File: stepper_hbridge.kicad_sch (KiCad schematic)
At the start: 20 parts, among them Q1 AO4264E, Q2 AO4264E, Q3 AO4264E, Q4 AO4264E

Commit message: Added symbol library
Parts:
- C2: value (none) -> 2.2n 50V; footprint (none) -> Capacitor_SMD:C_0603_1608Metric
- C5: value (none) -> 4.7uF 100V; footprint (none) -> Capacitor_SMD:C_1210_3225Metric
- Q1, Q3, Q4: symbol PersonnalSymbolLibrary:AO4264E -> QuarkCncStepperDrivers:AO4264E
- Q2: value AO4264E -> (none); symbol PersonnalSymbolLibrary:AO4264E -> QuarkCncStepperDrivers:AO4264E
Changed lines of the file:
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@@
     (stroke (width 0) (type default) (color 0 0 0 0))
   )
-  (text "Size up to 1206" (at 95.25 48.26 0)
+  (text "Size up to 1206" (at 95.25 46.99 0)
     (effects (font (size 1.27 1.27)) (justify left bottom))
   )
@@
     (effects (font (size 1.27 1.27)) (justify left bottom))
   )
-  (text "Average Pdiss of\n sense resistor\n     0.1 W" (at 95.25 57.15 0)
+  (text "Average Pdiss of\n sense resistor\n     0.1 W" (at 95.25 55.88 0)
     (effects (font (size 1.27 1.27)) (justify left bottom))
   )
@@
       (effects (font (size 1.27 1.27)) (justify left))
     )
-    (property "Value" "" (id 1) (at 97.79 102.2349 0)
-      (effects (font (size 1.27 1.27)) (justify left))
-    )
-    (property "Footprint" "" (id 2) (at 94.9452 104.14 0)
+    (property "Value" "2.2n 50V" (id 1) (at 97.79 102.2349 0)
+      (effects (font (size 1.27 1.27)) (justify left))
+    )
+    (property "Footprint" "Capacitor_SMD:C_0603_1608Metric" (id 2) (at 94.9452 104.14 0)
       (effects (font (size 1.27 1.27)) hide)
     )
@@
     (pin "2")
   )
-  (symbol (lib_id "PersonnalSymbolLibrary:AO4264E") (at 113.03 80.01 0) (unit 1)
+  (symbol (lib_id "QuarkCncStepperDrivers:AO4264E") (at 113.03 80.01 0) (unit 1)
     (in_bom yes) (on_board yes)
     (property "Reference" "Q2" (id 0) (at 116.84 76.1999 0)
       (effects (font (size 1.27 1.27)) (justify left))
     )
-    (property "Value" "AO4264E" (id 1) (at 116.84 83.8199 0)
+    (property "Value" "" (id 1) (at 116.84 83.8199 0)
       (effects (font (size 1.27 1.27)) (justify left))
     )
@@
       (effects (font (size 1.27 1.27)) (justify left) hide)
     )
-    (property "LCSC" "C334232" (id 4) (at 104.14 85.0899 0)
-      (effects (font (size 1.27 1.27)) (justify left) hide)
+    (property "LCSC" "C334232" (id 4) (at 113.03 80.01 0)
+      (effects (font (size 1.27 1.27)) hide)
     )
     (pin "1")
@@
       (effects (font (size 1.27 1.27)) (justify left))
     )
-    (property "Value" "" (id 1) (at 175.26 59.0549 0)
-      (effects (font (size 1.27 1.27)) (justify left))
-    )
-    (property "Footprint" "" (id 2) (at 172.4152 60.96 0)
+    (property "Value" "4.7uF 100V" (id 1) (at 175.26 59.0549 0)
+      (effects (font (size 1.27 1.27)) (justify left))
+    )
+    (property "Footprint" "Capacitor_SMD:C_1210_3225Metric" (id 2) (at 172.4152 60.96 0)
       (effects (font (size 1.27 1.27)) hide)
     )
@@
     (pin "2")
   )
-  (symbol (lib_id "PersonnalSymbolLibrary:AO4264E") (at 113.03 64.77 0) (unit 1)
+  (symbol (lib_id "QuarkCncStepperDrivers:AO4264E") (at 113.03 64.77 0) (unit 1)
     (in_bom yes) (on_board yes)
     (property "Reference" "Q1" (id 0) (at 116.84 60.9599 0)
@@
       (effects (font (size 1.27 1.27)) (justify left) hide)
     )
-    (property "LCSC" "C334232" (id 4) (at 104.14 68.5799 0)
-      (effects (font (size 1.27 1.27)) (justify left) hide)
+    (property "LCSC" "C334232" (id 4) (at 113.03 64.77 0)
+      (effects (font (size 1.27 1.27)) hide)
     )
     (pin "1")
@@
     (pin "2")
   )
-  (symbol (lib_id "PersonnalSymbolLibrary:AO4264E") (at 149.86 64.77 0) (unit 1)
+  (symbol (lib_id "QuarkCncStepperDrivers:AO4264E") (at 149.86 64.77 0) (unit 1)
     (in_bom yes) (on_board yes)
     (property "Reference" "Q3" (id 0) (at 147.32 60.9599 0)
@@
       (effects (font (size 1.27 1.27)) (justify left) hide)
     )
-    (property "LCSC" "C334232" (id 4) (at 156.21 67.3099 0)
-      (effects (font (size 1.27 1.27)) (justify left) hide)
+    (property "LCSC" "C334232" (id 4) (at 149.86 64.77 0)
+      (effects (font (size 1.27 1.27)) hide)
     )
     (pin "1")
@@
     (pin "2")
   )
-  (symbol (lib_id "PersonnalSymbolLibrary:AO4264E") (at 149.86 80.01 0) (unit 1)
+  (symbol (lib_id "QuarkCncStepperDrivers:AO4264E") (at 149.86 80.01 0) (unit 1)
     (in_bom yes) (on_board yes)
     (property "Reference" "Q4" (id 0) (at 147.32 76.1999 0)
@@
       (effects (font (size 1.27 1.27)) (justify left) hide)
     )
-    (property "LCSC" "C334232" (id 4) (at 156.21 82.5499 0)
-      (effects (font (size 1.27 1.27)) (justify left) hide)
-    )
-    (pin "1")
+    (property "LCSC" "C334232" (id 4) (at 149.86 80.01 0)
+      (effects (font (size 1.27 1.27)) hide)
+    )
+    (pin "1")

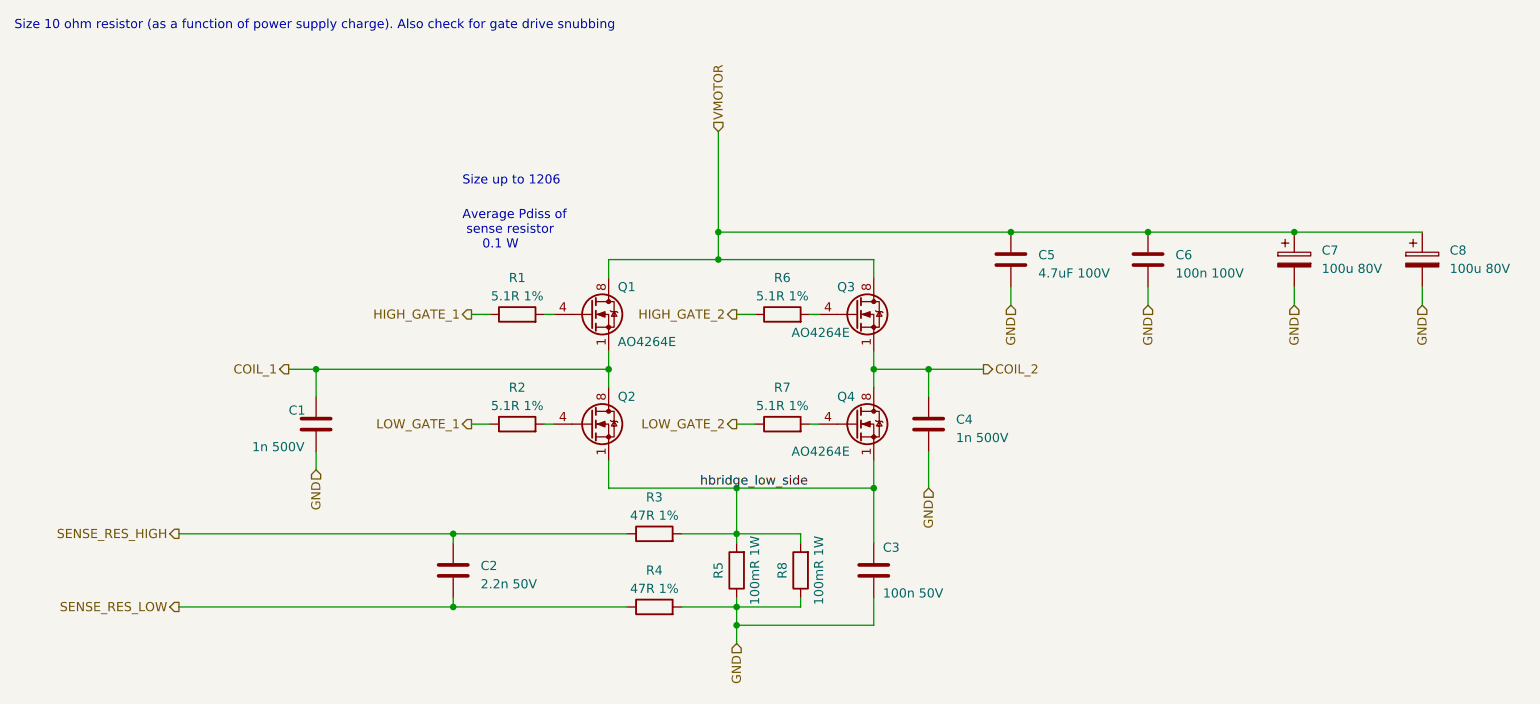
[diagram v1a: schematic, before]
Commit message: Removed caps from board. Will be placed on main board
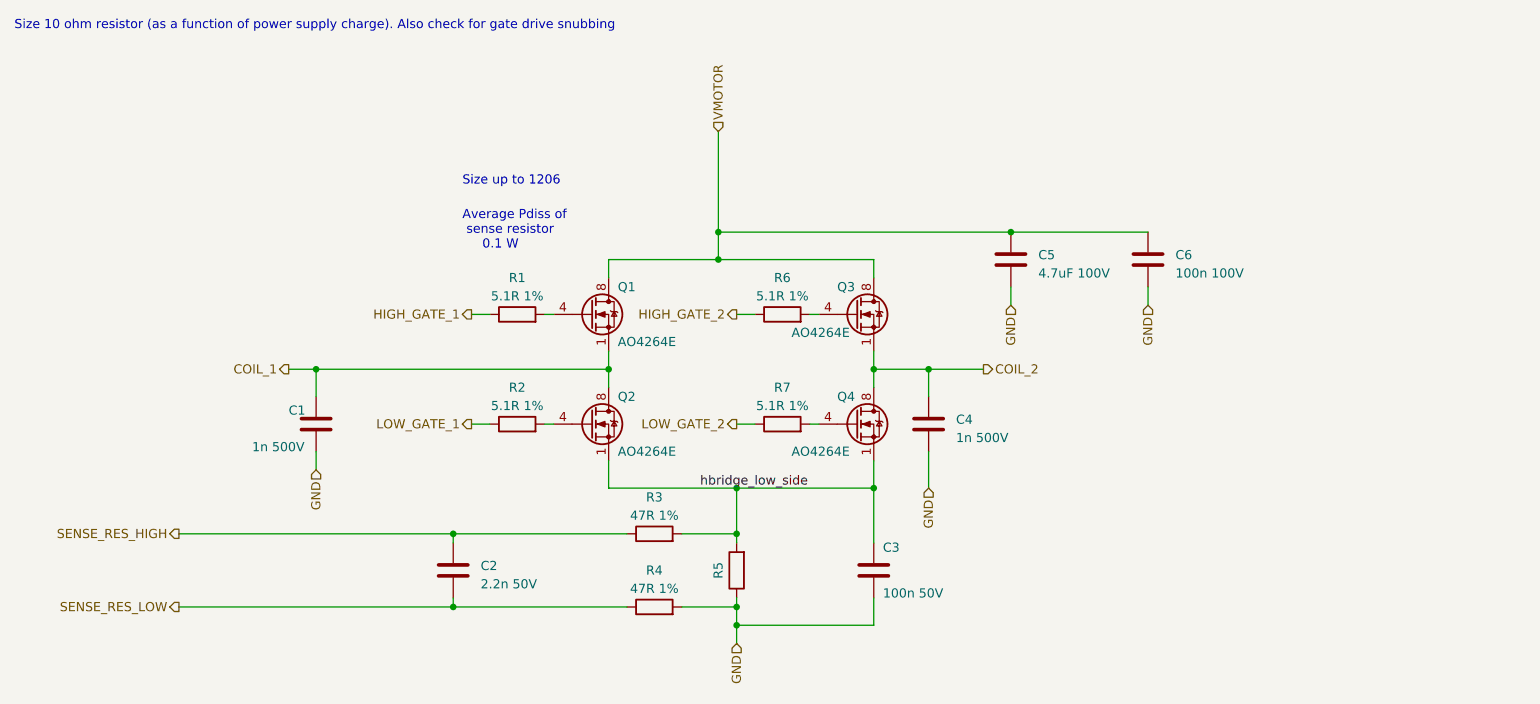
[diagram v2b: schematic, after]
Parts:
- removed C7, C8: 100u 80V, Capacitor_SMD:CP_Elec_10x10, symbol Device:C_Polarized
- removed R8: 100mR 1W, Resistor_SMD:R_1218_3246Metric, symbol Device:R
- Q2: value (none) -> AO4264E
- R5: value 100mR 1W -> (none); footprint Resistor_SMD:R_1218_3246Metric -> (none); LCSC C309639 -> C493478
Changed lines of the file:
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@@
   (junction (at 93.98 95.25) (diameter 0) (color 0 0 0 0)
   )
-  (junction (at 190.5 53.34) (diameter 0) (color 0 0 0 0)
-  )
   (junction (at 74.93 72.39) (diameter 0) (color 0 0 0 0)
   )
@@
   (junction (at 133.35 95.25) (diameter 0.9144) (color 0 0 0 0)
   )
-  (junction (at 210.82 53.34) (diameter 0) (color 0 0 0 0)
-  )
   (junction (at 93.98 105.41) (diameter 0) (color 0 0 0 0)
   )
@@
     (stroke (width 0) (type solid) (color 0 0 0 0))
   )
-  (wire (pts (xy 190.5 53.34) (xy 210.82 53.34))
-    (stroke (width 0) (type default) (color 0 0 0 0))
-  )
   (wire (pts (xy 130.81 57.15) (xy 152.4 57.15))
     (stroke (width 0) (type solid) (color 0 0 0 0))
   )
-  (wire (pts (xy 142.24 95.25) (xy 133.35 95.25))
-    (stroke (width 0) (type default) (color 0 0 0 0))
-  )
-  (wire (pts (xy 142.24 96.52) (xy 142.24 95.25))
-    (stroke (width 0) (type default) (color 0 0 0 0))
-  )
   (wire (pts (xy 115.57 57.15) (xy 130.81 57.15))
     (stroke (width 0) (type solid) (color 0 0 0 0))
@@
     (stroke (width 0) (type default) (color 0 0 0 0))
   )
-  (wire (pts (xy 210.82 53.34) (xy 228.6 53.34))
-    (stroke (width 0) (type default) (color 0 0 0 0))
-  )
   (wire (pts (xy 125.73 95.25) (xy 133.35 95.25))
     (stroke (width 0) (type solid) (color 0 0 0 0))
   )
-  (wire (pts (xy 228.6 60.96) (xy 228.6 63.5))
-    (stroke (width 0) (type default) (color 0 0 0 0))
-  )
   (wire (pts (xy 55.88 105.41) (xy 93.98 105.41))
     (stroke (width 0) (type solid) (color 0 0 0 0))
@@
   (wire (pts (xy 115.57 85.09) (xy 115.57 88.9))
     (stroke (width 0) (type solid) (color 0 0 0 0))
-  )
-  (wire (pts (xy 142.24 104.14) (xy 142.24 105.41))
-    (stroke (width 0) (type default) (color 0 0 0 0))
-  )
-  (wire (pts (xy 142.24 105.41) (xy 133.35 105.41))
-    (stroke (width 0) (type default) (color 0 0 0 0))
-  )
-  (wire (pts (xy 210.82 60.96) (xy 210.82 63.5))
-    (stroke (width 0) (type default) (color 0 0 0 0))
   )
   (wire (pts (xy 125.73 105.41) (xy 133.35 105.41))
@@
     (effects (font (size 1.27 1.27)) (justify right))
   )
-  (hierarchical_label "GND" (shape input) (at 228.6 63.5 270)
-    (effects (font (size 1.27 1.27)) (justify right))
-  )
   (hierarchical_label "HIGH_GATE_1" (shape output) (at 96.52 64.77 180)
     (effects (font (size 1.27 1.27)) (justify right))
@@
   (hierarchical_label "VMOTOR" (shape input) (at 130.81 39.37 90)
     (effects (font (size 1.27 1.27)) (justify left))
-  )
-  (hierarchical_label "GND" (shape input) (at 210.82 63.5 270)
-    (effects (font (size 1.27 1.27)) (justify right))
   )
   (hierarchical_label "COIL_2" (shape output) (at 167.64 72.39 0)
@@
       (effects (font (size 1.27 1.27)) (justify left))
     )
-    (property "Value" "" (id 1) (at 116.84 83.8199 0)
+    (property "Value" "AO4264E" (id 1) (at 116.84 83.8199 0)
       (effects (font (size 1.27 1.27)) (justify left))
     )
@@
     (in_bom yes) (on_board yes)
     (property "Reference" "R5" (id 0) (at 130.81 100.33 90))
-    (property "Value" "100mR 1W" (id 1) (at 135.89 100.33 90))
-    (property "Footprint" "Resistor_SMD:R_1218_3246Metric" (id 2) (at 135.128 100.33 90)
+    (property "Value" "" (id 1) (at 135.89 100.33 90))
+    (property "Footprint" "" (id 2) (at 135.128 100.33 90)
       (effects (font (size 1.27 1.27)) hide)
     )
@@
       (effects (font (size 1.27 1.27)) hide)
     )
-    (property "LCSC" "C309639" (id 4) (at 133.35 100.33 90)
+    (property "LCSC" "C493478" (id 4) (at 133.35 100.33 90)
       (effects (font (size 1.27 1.27)) hide)
     )
@@
     )
     (property "LCSC" "C307331" (id 4) (at 152.4 100.33 0)
-      (effects (font (size 1.27 1.27)) hide)
-    )
-    (pin "1")
-    (pin "2")
-  )
-  (symbol (lib_id "Device:C_Polarized") (at 228.6 57.15 0) (unit 1)
-    (in_bom yes) (on_board yes) (fields_autoplaced)
-    (property "Reference" "C8" (id 0) (at 232.41 55.8799 0)
-      (effects (font (size 1.27 1.27)) (justify left))
-    )
-    (property "Value" "100u 80V" (id 1) (at 232.41 58.4199 0)
-      (effects (font (size 1.27 1.27)) (justify left))
-    )
-    (property "Footprint" "Capacitor_SMD:CP_Elec_10x10" (id 2) (at 229.5652 60.96 0)
-      (effects (font (size 1.27 1.27)) hide)
-    )
-    (property "Datasheet" "~" (id 3) (at 228.6 57.15 0)
-      (effects (font (size 1.27 1.27)) hide)
-    )
-    (property "LCSC" "C487410" (id 4) (at 228.6 57.15 0)
       (effects (font (size 1.27 1.27)) hide)
     )
@@
     (pin "8")
   )
-  (symbol (lib_id "Device:C_Polarized") (at 210.82 57.15 0) (unit 1)
-    (in_bom yes) (on_board yes) (fields_autoplaced)
-    (property "Reference" "C7" (id 0) (at 214.63 55.8799 0)
-      (effects (font (size 1.27 1.27)) (justify left))
-    )
-    (property "Value" "100u 80V" (id 1) (at 214.63 58.4199 0)
-      (effects (font (size 1.27 1.27)) (justify left))
-    )
-    (property "Footprint" "Capacitor_SMD:CP_Elec_10x10" (id 2) (at 211.7852 60.96 0)
-      (effects (font (size 1.27 1.27)) hide)
-    )
-    (property "Datasheet" "~" (id 3) (at 210.82 57.15 0)
-      (effects (font (size 1.27 1.27)) hide)
-    )
-    (property "LCSC" "C487410" (id 4) (at 210.82 57.15 0)
-      (effects (font (size 1.27 1.27)) hide)
-    )
-    (pin "1")
-    (pin "2")
-  )
   (symbol (lib_id "Device:R") (at 102.87 80.01 90) (unit 1)
     (in_bom yes) (on_board yes)
@@
       (effects (font (size 1.27 1.27)) hide)
     )
-    (pin "1")
-    (pin "2")
-  )
-  (symbol (lib_id "Device:R") (at 142.24 100.33 180) (unit 1)
-    (in_bom yes) (on_board yes)
-    (property "Reference" "R8" (id 0) (at 139.7 100.33 90))
-    (property "Value" "100mR 1W" (id 1) (at 144.78 100.33 90))
-    (property "Footprint" "Resistor_SMD:R_1218_3246Metric" (id 2) (at 144.018 100.33 90)
-      (effects (font (size 1.27 1.27)) hide)
-    )
-    (property "Datasheet" "~" (id 3) (at 142.24 100.33 0)
-      (effects (font (size 1.27 1.27)) hide)
-    )
-    (property "LCSC" "C309639" (id 4) (at 142.24 100.33 90)
-      (effects (font (size 1.27 1.27)) hide)
-    )

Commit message: Removed 0Ohms. Keyed design
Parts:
- R5: value (none) -> 30mR 2W; footprint (none) -> Resistor_SMD:R_2512_6332Metric
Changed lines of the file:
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@@
     (in_bom yes) (on_board yes)
     (property "Reference" "R5" (id 0) (at 130.81 100.33 90))
-    (property "Value" "" (id 1) (at 135.89 100.33 90))
-    (property "Footprint" "" (id 2) (at 135.128 100.33 90)
+    (property "Value" "30mR 2W" (id 1) (at 135.89 100.33 90))
+    (property "Footprint" "Resistor_SMD:R_2512_6332Metric" (id 2) (at 135.128 100.33 90)
       (effects (font (size 1.27 1.27)) hide)
     )
